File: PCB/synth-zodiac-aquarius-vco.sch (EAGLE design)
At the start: 59 parts, among them Q1 PMP4201, U3 LM393, U4 TL074A, U5 CD4066

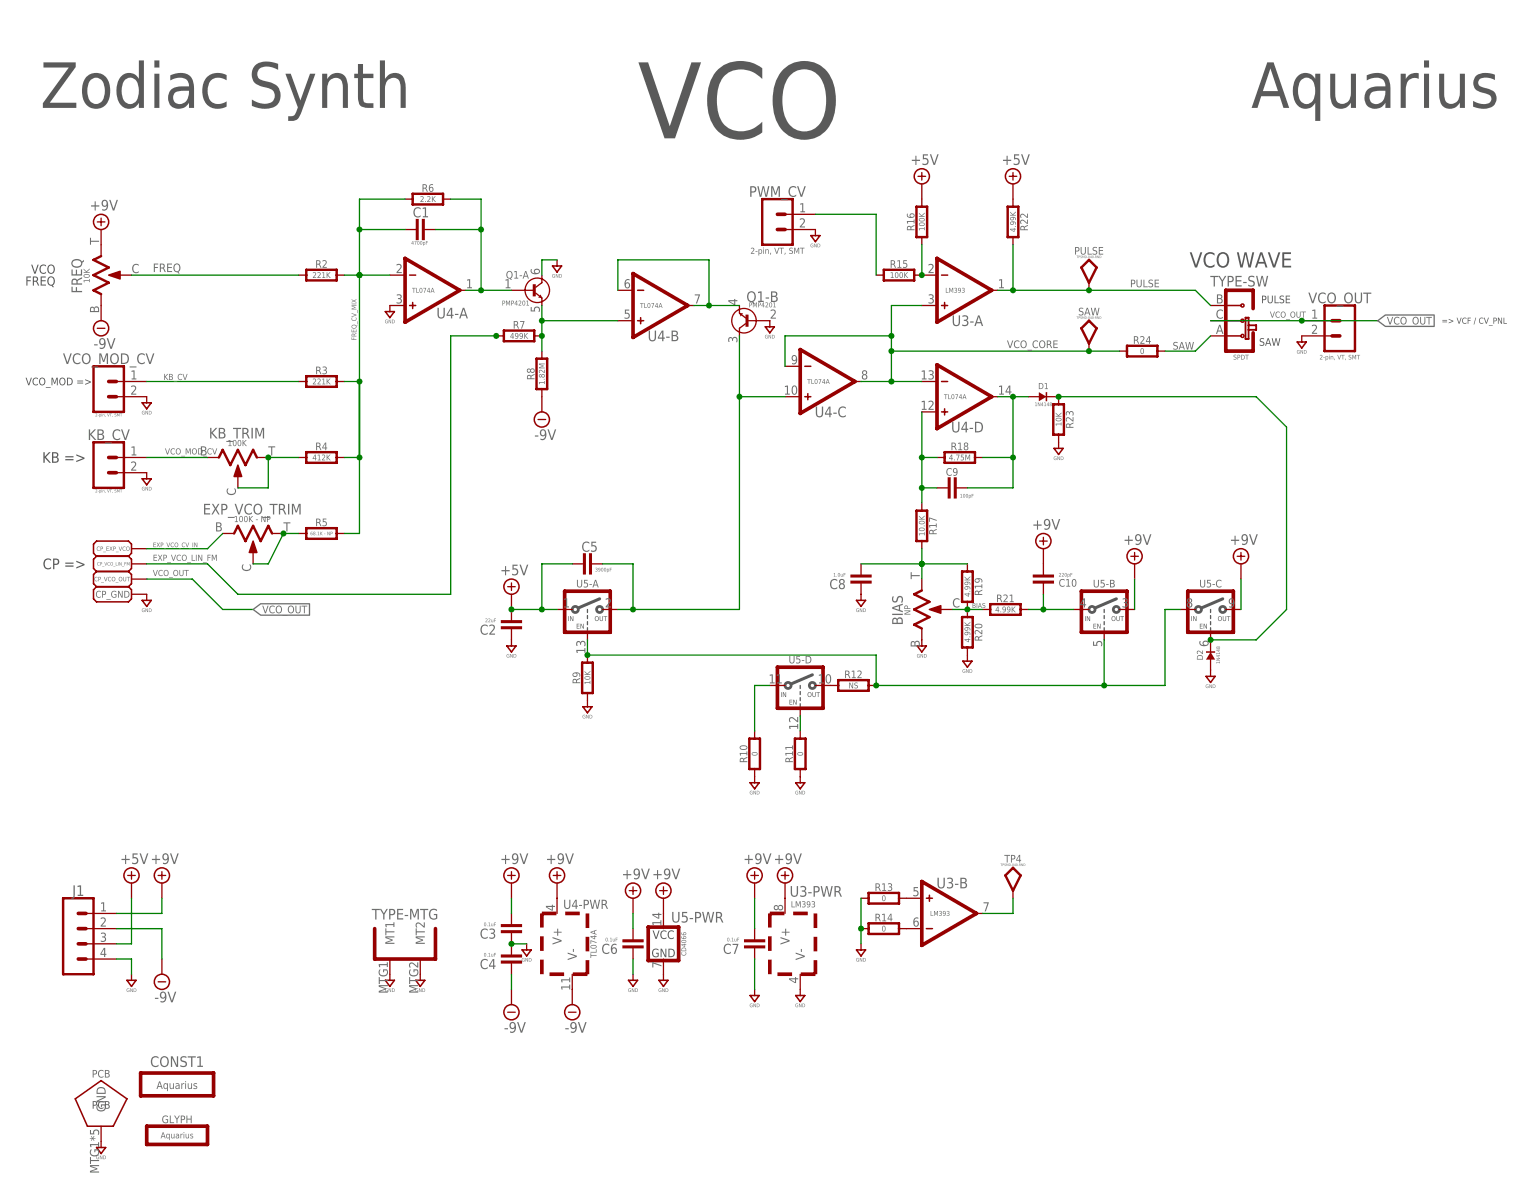
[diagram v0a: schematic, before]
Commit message: Almost ready for FAB.
Sagittarius was mis-spelled, renamed it.  Taurus is still WIP.
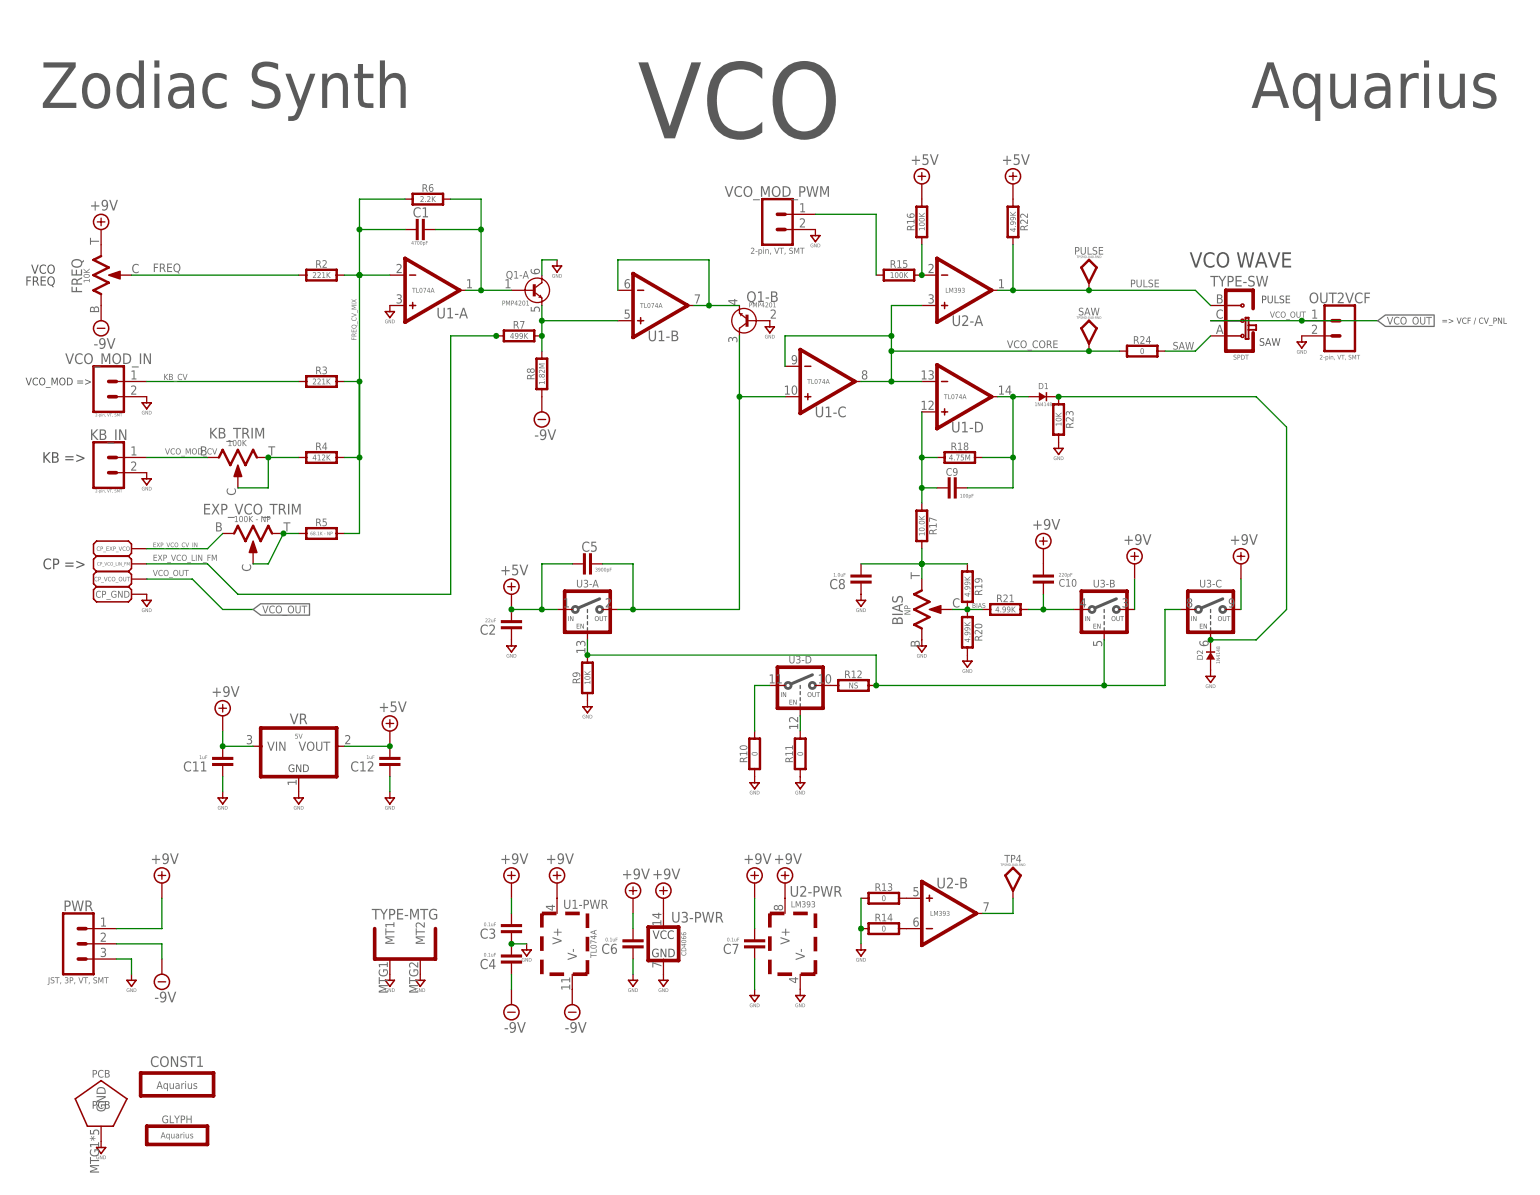
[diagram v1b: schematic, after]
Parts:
- removed J1: (no value), con-jst:04P-VT-SMT
- removed U5: CD4066, logic:CD4066SO14
- added C11, C12: 1uF, rlc:CAPACITOR0603
- added PWR: JST, 3P, VT, SMT, con-jst:03P-VT-SMT
- added U2: LM393, op-amp:DUAL-LM393ED
- added VR: 5V, regulators:LDO-3P--5V-SOT23
- U3: value LM393 -> CD4066; device op-amp:DUAL-LM393ED -> logic:CD4066SO14
- renumbered KB_CV to KB_IN, PWM_CV to VCO_MOD_PWM, U4 to U1, VCO_MOD_CV to VCO_MOD_IN, VCO_OUT to OUT2VCF
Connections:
- net +5V: now also C12.2, U3-A.IN, VR.VOUT; no longer J1.3, U5-A.IN
- net +9V: now also C11.2, PWR.1, U2-PWR.V+, U3-B.OUT, U3-C.OUT, U3-PWR.VCC, VR.VIN; no longer J1.1, U3-PWR.V+, U5-B.OUT, U5-C.OUT, U5-PWR.VCC
- net -9V: now also PWR.2; no longer J1.2
- net GND: now also C11.1, C12.1, PWR.3, U2-PWR.V-, U3-PWR.GND, VR.GND; no longer J1.4, U3-PWR.V-, U5-PWR.GND
- net N$15: now also U3-A.EN, U3-B.EN, U3-C.IN; no longer U5-A.EN, U5-B.EN, U5-C.IN
- net N$17: now also U2-B.-; no longer U3-B.-
- net N$20: now also U3-A.OUT; no longer U5-A.OUT
- net N$22: now also U3-B.IN; no longer U5-B.IN
- net N$23: now also U3-D.OUT; no longer U5-D.OUT
- net N$24: now also U3-C.EN; no longer U5-C.EN
- net N$25: now also U3-D.IN; no longer U5-D.IN
- net N$26: now also U3-D.EN; no longer U5-D.EN
- net N$27: now also U2-B.+; no longer U3-B.+
- net N$28: now also U2-A.-; no longer U3-A.-
- net N$29: now also U2-B.OUT; no longer U3-B.OUT
- net PULSE: now also U2-A.OUT; no longer U3-A.OUT
- net VCO_CORE: now also U2-A.+; no longer U3-A.+
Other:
- moved on the sheet: U3-PWR

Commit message: Work in progress for rev A,  VCO rev.B
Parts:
- removed CONST1: Aquarius, circuit-monkey-zodiac:CONSTELLATION-AQUARIUS
- removed CP_EXP_VCO, CP_GND, CP_VCO_LIN_FM, CP_VCO_OUT: PADSMD-070X070, con-testpoints:PADSMD-070X070
- removed EXP_VCO_TRIM: 100K - NP, rlc:TRIMPOTTC33X
- removed R24: 0, rlc:RESISTOR0603
- removed TYPE: SPDT, switch-thd:SLIDE-SPDTSS-12-F45-TH-PCB
- added CONST: Aquarius, circuit-monkey-zodiac:CONSTELLATION-AQUARIUS
- added F_0-5, F_GND: PADSMD-070X070, con-testpoints:PADSMD-070X070
- added MODE: (no value), switch-thd:SLIDE-SPDT-MNTSS-12-F45-TH-PCB
- added R1: 150K, rlc:RESISTOR0603
- KB_IN, OUT2VCF, VCO_MOD_IN, VCO_MOD_PWM: value 2-pin, VT, SMT -> JST, SH, 2P; device con-jst:02PVT-SMT -> con-jst:02P-SM-VT-SMT
- PWR: value JST, 3P, VT, SMT -> JST SM 3P; device con-jst:03P-VT-SMT -> con-jst:03P-SM-VT-SMT
- R5: value 68.1K - NP -> 150K
- R7: value 499K -> 47K
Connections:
- removed net EXP_VCO_CV_IN: CP_EXP_VCO.PAD, EXP_VCO_TRIM.1
- removed net EXP_VCO_LIN_FM: CP_VCO_LIN_FM.PAD, R7.1
- removed net N$9: EXP_VCO_TRIM.2, EXP_VCO_TRIM.3, R5.1
- removed net VCO_CORE: R24.1, SAW.P$1, U1-C.-, U1-C.OUT, U1-D.-, U2-A.+
- new net FREQ_5: F_0-5.PAD, R1.1, R5.2, R7.2
- net +9V: now also R1.2
- net FREQ: now also R5.1
- net FREQ_CV_MIX: no longer R5.2
- net GND: now also F_GND.PAD, MODE-MTG.MT1, MODE-MTG.MT2, R7.1; no longer CP_GND.PAD, TYPE-MTG.MT1, TYPE-MTG.MT2
- net N$12: no longer R7.2
- net PULSE: now also MODE-SW.B; no longer TYPE-SW.B
- net SAW: now also MODE-SW.A, SAW.P$1, U1-C.-, U1-C.OUT, U1-D.-, U2-A.+; no longer R24.2, TYPE-SW.A
- net VCO_OUT: now also MODE-SW.C; no longer CP_VCO_OUT.PAD, TYPE-SW.C
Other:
- note added: "Convert -9 to +9 range to 0-3.3V for LED PCB."
- note added: "SATAN'S CYCLE WORKS"
- note added: "TO LED BOARD"
- note removed: "=> VCF / CV_PNL"
- note removed: "CP =>"
- moved on the sheet: BIAS, C1, C10, C11, C12, C2, C3, C4, C5, C6, C7, C8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

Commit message: Perhaps final Rev. A?
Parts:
- MODE: device switch-thd:SLIDE-SPDT-MNTSS-12-F45-TH-PCB -> switch-thd:SLIDE-SPDT-MNTSS-12-F45-TH-PCB-2
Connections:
- net PULSE: now also MODE-SW.A; no longer MODE-SW.B
- net SAW: now also MODE-SW.B; no longer MODE-SW.A
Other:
- moved on the sheet: MODE-MTG, MODE-SW

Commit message: Tune values and some schematic visual tweaks.
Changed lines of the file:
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@@
 <grid distance="0.1" unitdist="inch" unit="inch" style="lines" multiple="1" display="no" altdistance="0.01" altunitdist="inch" altunit="inch"/>
 <layers>
-<layer number="1" name="Top" color="4" fill="1" visible="yes" active="no"/>
-<layer number="2" name="Route2" color="16" fill="1" visible="yes" active="no"/>
-<layer number="3" name="Route3" color="17" fill="1" visible="yes" active="no"/>
-<layer number="4" name="Route4" color="18" fill="1" visible="yes" active="no"/>
-<layer number="5" name="Route5" color="19" fill="1" visible="yes" active="no"/>
-<layer number="6" name="Route6" color="25" fill="1" visible="yes" active="no"/>
-<layer number="7" name="Route7" color="26" fill="1" visible="yes" active="no"/>
-<layer number="8" name="Route8" color="27" fill="1" visible="yes" active="no"/>
-<layer number="9" name="Route9" color="28" fill="1" visible="yes" active="no"/>
-<layer number="10" name="Route10" color="29" fill="1" visible="yes" active="no"/>
-<layer number="11" name="Route11" color="30" fill="1" visible="yes" active="no"/>
-<layer number="12" name="Route12" color="20" fill="1" visible="yes" active="no"/>
-<layer number="13" name="Route13" color="21" fill="1" visible="yes" active="no"/>
-<layer number="14" name="Route14" color="22" fill="1" visible="yes" active="no"/>
-<layer number="15" name="Route15" color="23" fill="1" visible="yes" active="no"/>
-<layer number="16" name="Bottom" color="1" fill="1" visible="yes" active="no"/>
-<layer number="17" name="Pads" color="2" fill="1" visible="yes" active="no"/>
-<layer number="18" name="Vias" color="2" fill="1" visible="yes" active="no"/>
-<layer number="19" name="Unrouted" color="6" fill="1" visible="yes" active="no"/>
-<layer number="20" name="Dimension" color="24" fill="1" visible="yes" active="no"/>
-<layer number="21" name="tPlace" color="7" fill="1" visible="yes" active="no"/>
-<layer number="22" name="bPlace" color="7" fill="1" visible="yes" active="no"/>
-<layer number="23" name="tOrigins" color="15" fill="1" visible="yes" active="no"/>
-<layer number="24" name="bOrigins" color="15" fill="1" visible="yes" active="no"/>
-<layer number="25" name="tNames" color="7" fill="1" visible="yes" active="no"/>
-<layer number="26" name="bNames" color="7" fill="1" visible="yes" active="no"/>
-<layer number="27" name="tValues" color="7" fill="1" visible="yes" active="no"/>
-<layer number="28" name="bValues" color="7" fill="1" visible="yes" active="no"/>
+<layer number="1" name="Top" color="4" fill="1" visible="no" active="no"/>
+<layer number="2" name="Route2" color="16" fill="1" visible="no" active="no"/>
+<layer number="3" name="Route3" color="17" fill="1" visible="no" active="no"/>
+<layer number="4" name="Route4" color="18" fill="1" visible="no" active="no"/>
+<layer number="5" name="Route5" color="19" fill="1" visible="no" active="no"/>
+<layer number="6" name="Route6" color="25" fill="1" visible="no" active="no"/>
+<layer number="7" name="Route7" color="26" fill="1" visible="no" active="no"/>
+<layer number="8" name="Route8" color="27" fill="1" visible="no" active="no"/>
+<layer number="9" name="Route9" color="28" fill="1" visible="no" active="no"/>
+<layer number="10" name="Route10" color="29" fill="1" visible="no" active="no"/>
+<layer number="11" name="Route11" color="30" fill="1" visible="no" active="no"/>
+<layer number="12" name="Route12" color="20" fill="1" visible="no" active="no"/>
+<layer number="13" name="Route13" color="21" fill="1" visible="no" active="no"/>
+<layer number="14" name="Route14" color="22" fill="1" visible="no" active="no"/>
+<layer number="15" name="Route15" color="23" fill="1" visible="no" active="no"/>
+<layer number="16" name="Bottom" color="1" fill="1" visible="no" active="no"/>
+<layer number="17" name="Pads" color="2" fill="1" visible="no" active="no"/>
+<layer number="18" name="Vias" color="2" fill="1" visible="no" active="no"/>
+<layer number="19" name="Unrouted" color="6" fill="1" visible="no" active="no"/>
+<layer number="20" name="Dimension" color="24" fill="1" visible="no" active="no"/>
+<layer number="21" name="tPlace" color="7" fill="1" visible="no" active="no"/>
+<layer number="22" name="bPlace" color="7" fill="1" visible="no" active="no"/>
+<layer number="23" name="tOrigins" color="15" fill="1" visible="no" active="no"/>
+<layer number="24" name="bOrigins" color="15" fill="1" visible="no" active="no"/>
+<layer number="25" name="tNames" color="7" fill="1" visible="no" active="no"/>
+<layer number="26" name="bNames" color="7" fill="1" visible="no" active="no"/>
+<layer number="27" name="tValues" color="7" fill="1" visible="no" active="no"/>
+<layer number="28" name="bValues" color="7" fill="1" visible="no" active="no"/>
 <layer number="29" name="tStop" color="7" fill="3" visible="no" active="no"/>
 <layer number="30" name="bStop" color="7" fill="6" visible="no" active="no"/>
@@
 <layer number="35" name="tGlue" color="7" fill="4" visible="no" active="no"/>
 <layer number="36" name="bGlue" color="7" fill="5" visible="no" active="no"/>
-<layer number="37" name="tTest" color="7" fill="1" visible="yes" active="no"/>
-<layer number="38" name="bTest" color="7" fill="1" visible="yes" active="no"/>
+<layer number="37" name="tTest" color="7" fill="1" visible="no" active="no"/>
+<layer number="38" name="bTest" color="7" fill="1" visible="no" active="no"/>
 <layer number="39" name="tKeepout" color="4" fill="11" visible="no" active="no"/>
 <layer number="40" name="bKeepout" color="1" fill="11" visible="no" active="no"/>
@@
 <layer number="44" name="Drills" color="7" fill="1" visible="no" active="no"/>
 <layer number="45" name="Holes" color="7" fill="1" visible="no" active="no"/>
-<layer number="46" name="Milling" color="3" fill="1" visible="yes" active="no"/>
-<layer number="47" name="Measures" color="7" fill="1" visible="yes" active="no"/>
-<layer number="48" name="Document" color="7" fill="1" visible="yes" active="no"/>
-<layer number="49" name="Reference" color="7" fill="1" visible="yes" active="no"/>
-<layer number="50" name="dxf" color="7" fill="1" visible="yes" active="no"/>
-<layer number="51" name="tDocu" color="61" fill="1" visible="yes" active="no"/>
-<layer number="52" name="bDocu" color="24" fill="1" visible="yes" active="no"/>
-<layer number="53" name="tGND_GNDA" color="7" fill="9" visible="yes" active="no"/>
-<layer number="54" name="bGND_GNDA" color="1" fill="9" visible="yes" active="no"/>
-<layer number="56" name="wert" color="7" fill="1" visible="yes" active="no"/>
-<layer number="57" name="tCAD" color="7" fill="1" visible="yes" active="no"/>
-<layer number="59" name="tCarbon" color="7" fill="1" visible="yes" active="no"/>
-<layer number="60" name="bCarbon" color="7" fill="1" visible="yes" active="no"/>
+<layer number="46" name="Milling" color="3" fill="1" visible="no" active="no"/>
+<layer number="47" name="Measures" color="7" fill="1" visible="no" active="no"/>
+<layer number="48" name="Document" color="7" fill="1" visible="no" active="no"/>
+<layer number="49" name="Reference" color="7" fill="1" visible="no" active="no"/>
+<layer number="50" name="dxf" color="7" fill="1" visible="no" active="no"/>
+<layer number="51" name="tDocu" color="61" fill="1" visible="no" active="no"/>
+<layer number="52" name="bDocu" color="24" fill="1" visible="no" active="no"/>
+<layer number="53" name="tGND_GNDA" color="7" fill="9" visible="no" active="no"/>
+<layer number="54" name="bGND_GNDA" color="1" fill="9" visible="no" active="no"/>
+<layer number="56" name="wert" color="7" fill="1" visible="no" active="no"/>
+<layer number="57" name="tCAD" color="7" fill="1" visible="no" active="no"/>
+<layer number="59" name="tCarbon" color="7" fill="1" visible="no" active="no"/>
+<layer number="60" name="bCarbon" color="7" fill="1" visible="no" active="no"/>
 <layer number="88" name="SimResults" color="9" fill="1" visible="yes" active="yes"/>
 <layer number="89" name="SimProbes" color="9" fill="1" visible="yes" active="yes"/>
@@
 <junction x="55.88" y="142.24"/>
 <label x="55.372" y="131.318" size="0.8128" layer="95" rot="R90"/>
+<junction x="55.88" y="124.46"/>
 </segment>
 </net>
